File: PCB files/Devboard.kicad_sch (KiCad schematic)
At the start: 37 parts, among them J1 USB_C_Receptacle_USB2.0_14P, J2 Conn_01x03, J3 Conn_01x20, J4 Conn_01x20, J5 JST_2mm_LiPo, SW1 SW_Push, U1 RP2040, U2 NCP1117-3.3_SOT223, U3 W25Q128JVS, Y1 12Mhz

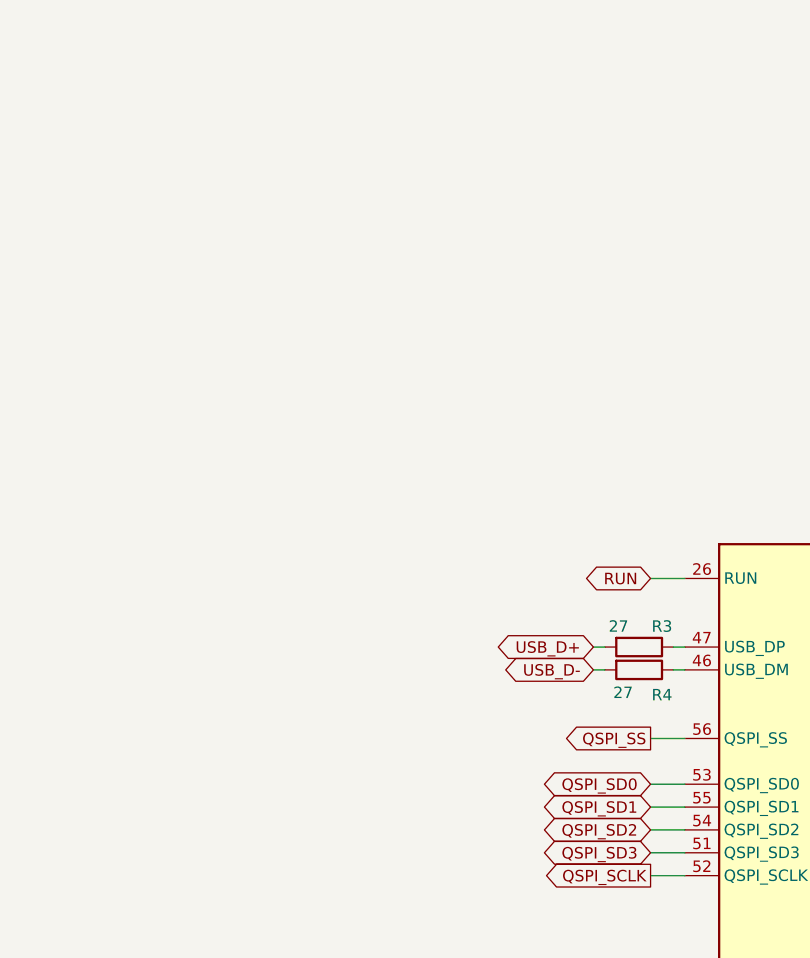
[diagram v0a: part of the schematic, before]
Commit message: added MPU-6500 IMU
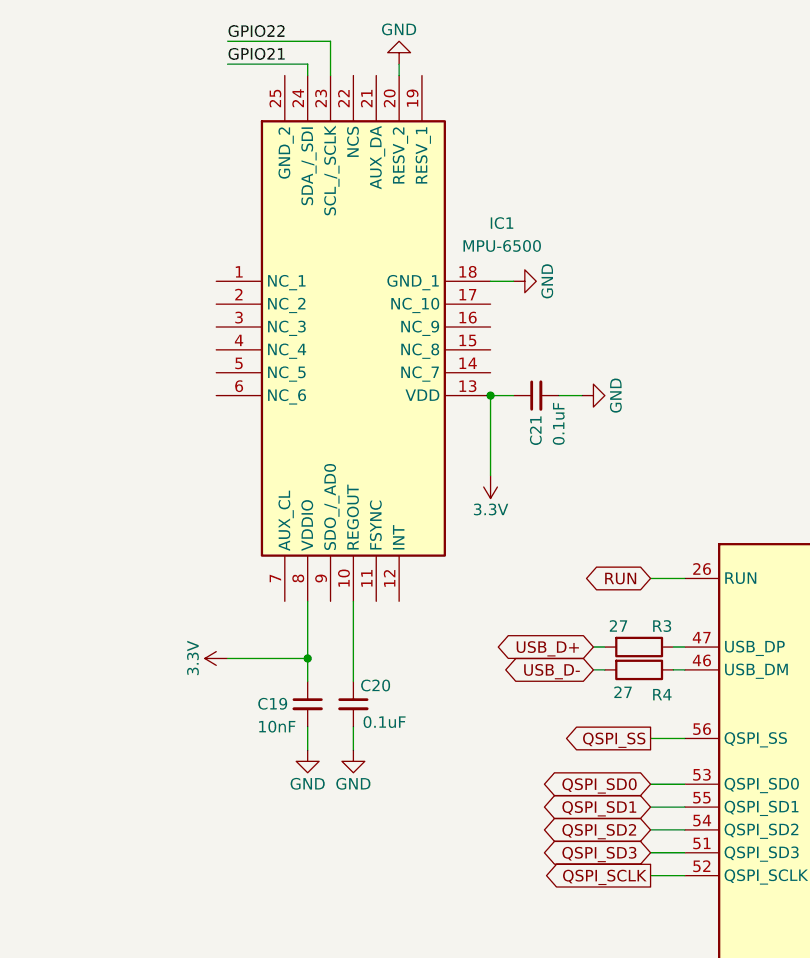
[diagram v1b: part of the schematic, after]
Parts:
- added C19: 10nF, PCM_SparkFun-Capacitor:C_0603_1608Metric, symbol PCM_SparkFun-Capacitor:C
- added C20, C21: 0.1uF, PCM_SparkFun-Capacitor:C_0603_1608Metric, symbol PCM_SparkFun-Capacitor:C
- added IC1: MPU-6500, KiCadMPU:QFN40P300X300X95-25N-D, symbol MPU-6500:MPU-6500
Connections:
- net 3.3V: now also C19.1, C21.1, IC1.13 (VDD), IC1.8 (VDDIO)
- net GND: now also C19.2, C20.2, C21.2, IC1.18 (GND_1), IC1.20 (RESV_2)
- net GPIO21: now also IC1.24 (SDA_/_SDI)
- net GPIO22: now also IC1.23 (SCL_/_SCLK)
- new net: C20.1, IC1.10 (REGOUT)
